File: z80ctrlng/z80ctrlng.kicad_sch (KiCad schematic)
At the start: 54 parts, among them J1 BUS, J10 QWIIC, J11 CLOCK, J2 MICRO_SD, J3 UEXT, J4 SERIAL, J5 3V_LINK, J6 UPDI, J7 UEXT_CS, J8 S1_LINK, J9 S2_LINK, Q4 BSS138, SW1 RESET, SW1 RTC, SW2 BANK_EN, U1 AVR128DB64x-xPT, U1 MCP7940N-xST, U2 MIC5504-3.3YM5, U5 74HCT574, U6 74HCT257, U7 AS6C4008-55PCN, Y1 32kHz

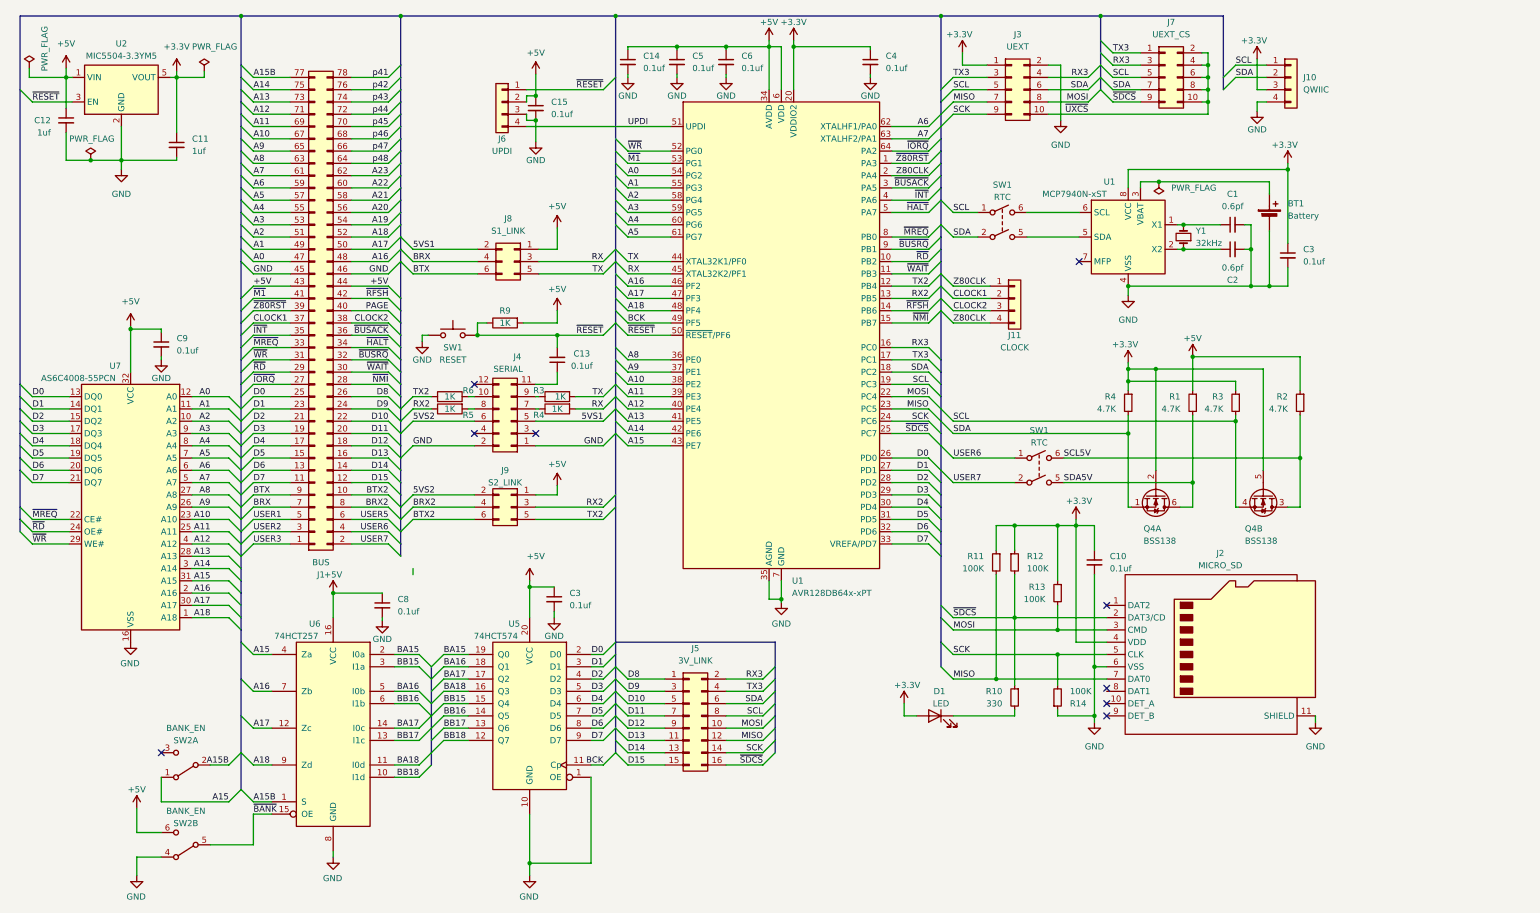
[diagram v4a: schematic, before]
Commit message: Switch to RCBus-80 footprints, JLCPCB preferred components
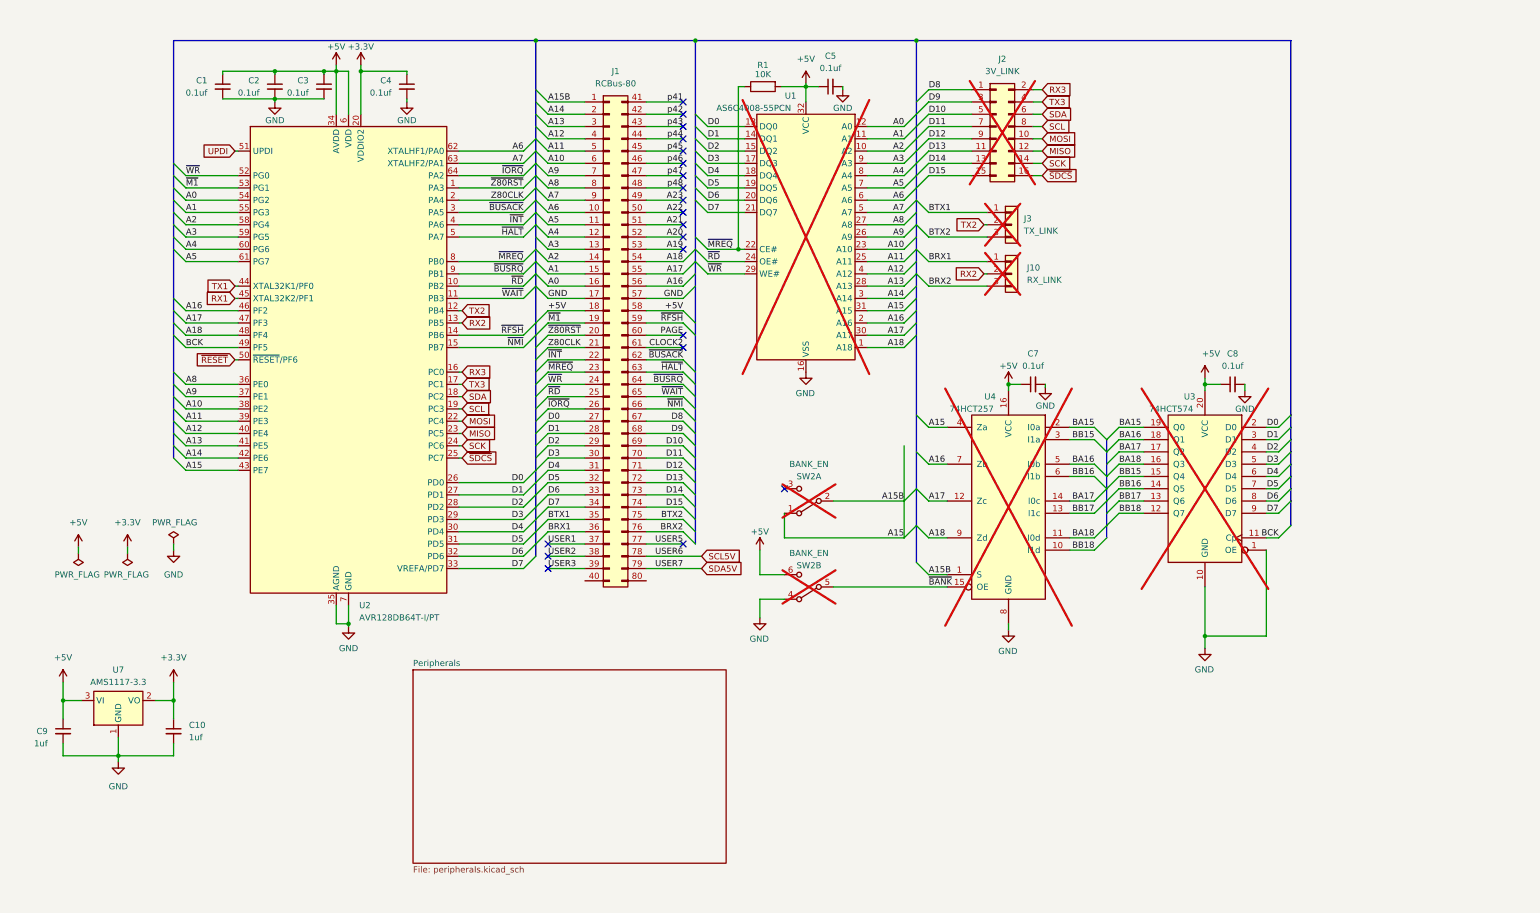
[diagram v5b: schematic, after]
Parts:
- removed BT1: Battery, Battery:BatteryHolder_Keystone_3001_1x12mm, symbol Device:Battery_Cell
- removed C1, C2: 0.6pf, Capacitor_SMD:C_0402_1005Metric, symbol Device:C_Small
- removed C11, C12: 1uf, Capacitor_SMD:C_0402_1005Metric, symbol Device:C_Small
- removed C13, C15, C3: 0.1uf, Capacitor_SMD:C_0402_1005Metric, symbol Device:C_Small
- removed D1: LED, LED_SMD:LED_0805_2012Metric, symbol Device:LED
- removed J1: BUS, Connector_PinHeader_2.54mm:PinHeader_2x39_P2.54mm_Horizontal, symbol Connector_Generic:Conn_02x39_Odd_Even
- removed J10: QWIIC, Custom:JST_SM04B-SRSS-TB_LF__SN_, symbol Connector_Generic:Conn_01x04
- removed J11: CLOCK, Connector_PinHeader_2.54mm:PinHeader_1x04_P2.54mm_Vertical, symbol Connector_Generic:Conn_01x04
- removed J2: MICRO_SD, Connector_Card:microSD_HC_Molex_104031-0811, symbol Connector:Micro_SD_Card_Det2
- removed J3: UEXT, Connector_IDC:IDC-Header_2x05_P2.54mm_Vertical, symbol Connector_Generic:Conn_02x05_Odd_Even
- removed J4: SERIAL, Connector_PinHeader_2.54mm:PinHeader_2x06_P2.54mm_Horizontal, symbol Connector_Generic:Conn_02x06_Odd_Even
- removed J6: UPDI, Connector_PinHeader_2.54mm:PinHeader_1x04_P2.54mm_Horizontal, symbol Connector_Generic:Conn_01x04
- removed J7: UEXT_CS, Connector_PinHeader_2.54mm:PinHeader_2x05_P2.54mm_Vertical, symbol Connector_Generic:Conn_02x05_Odd_Even
- removed J8: S1_LINK, Connector_PinHeader_2.54mm:PinHeader_2x03_P2.54mm_Vertical, symbol Connector_Generic:Conn_02x03_Odd_Even
- removed J9: S2_LINK, Connector_PinHeader_2.54mm:PinHeader_2x03_P2.54mm_Vertical, symbol Connector_Generic:Conn_02x03_Odd_Even
- removed Q4: BSS138, Package_TO_SOT_SMD:SOT-363_SC-70-6, symbol Transistor_FET:FDG6335N
- removed R1, R2, R3, R4: 4.7K, Resistor_SMD:R_0402_1005Metric, symbol Device:R_Small
- removed R10: 330, Resistor_SMD:R_0402_1005Metric, symbol Device:R_Small
- removed R11, R12, R13, R14: 100K, Resistor_SMD:R_0402_1005Metric, symbol Device:R_Small
- removed R3, R4, R5, R6, R9: 1K, Resistor_SMD:R_0402_1005Metric, symbol Device:R
- removed SW1: RESET, Button_Switch_THT:SW_PUSH_6mm, symbol Switch:SW_Push
- removed SW1 (x2): RTC, Custom:SWITCH_011CQN, symbol Switch:SW_DPST
- removed U1: MCP7940N-xST, Package_SO:TSSOP-8_3x3mm_P0.65mm, symbol Timer_RTC:MCP7940N-xST
- removed U2: MIC5504-3.3YM5, Package_TO_SOT_SMD:SOT-23-5, symbol Regulator_Linear:MIC5504-3.3YM5
- removed Y1: 32kHz, Crystal:Crystal_SMD_3215-2Pin_3.2x1.5mm, symbol Device:Crystal_Small
- added C9: 1uf, Capacitor_SMD:C_0402_1005Metric, symbol Device:C_Small
- added J1: RCBus-80, Custom:RCBus-80, symbol Connector_Generic:Conn_02x40_Top_Bottom
- added J10: RX_LINK, Connector_PinHeader_2.54mm:PinHeader_1x03_P2.54mm_Vertical, symbol Connector_Generic:Conn_01x03
- added J3: TX_LINK, Connector_PinHeader_2.54mm:PinHeader_1x03_P2.54mm_Vertical, symbol Connector_Generic:Conn_01x03
- added R1: 10K, Resistor_SMD:R_0402_1005Metric, symbol Device:R
- added U7: AMS1117-3.3, Package_TO_SOT_SMD:SOT-223-3_TabPin2, symbol Regulator_Linear:AMS1117-3.3
- C10: value 0.1uf -> 1uf
- J2: renamed from J5; now not fitted
- SW2: footprint Custom:SWITCH_011CQN -> SamacSys_Parts:JS202011CQN; now not fitted
- U1: renamed from U7; now not fitted
- U2: renamed from U1; value AVR128DB64x-xPT -> AVR128DB64T-I/PT
- U3: renamed from U5; now not fitted
- U4: renamed from U6; now not fitted
- renumbered C14 to C1, C5 to C2, C6 to C3, C9 to C5, C8 to C7, C3 to C8
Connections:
- net A15B is gone; now on net A15: SW2.2 (B), U4.1 (S)
- net +3.3V: now also U7.2 (VO)
- net +5V: now also C9.1, J1.18 (Pin_18), J1.58 (Pin_58), R1.2, U7.3 (VI)
- net A0: now also J1.16 (Pin_16)
- net A1: now also J1.15 (Pin_15)
- net A10: now also J1.6 (Pin_6)
- net A11: now also J1.5 (Pin_5)
- net A12: now also J1.4 (Pin_4)
- net A13: now also J1.3 (Pin_3)
- net A14: now also J1.2 (Pin_2)
- net A15: now also J1.1 (Pin_1)
- net A16: now also J1.56 (Pin_56)
- net A17: now also J1.55 (Pin_55)
- net A18: now also J1.54 (Pin_54)
- net A19: now also J1.53 (Pin_53)
- net A2: now also J1.14 (Pin_14)
- net A20: now also J1.52 (Pin_52)
- net A21: now also J1.51 (Pin_51)
- net A22: now also J1.50 (Pin_50)
- net A23: now also J1.49 (Pin_49)
- net A3: now also J1.13 (Pin_13)
- net A4: now also J1.12 (Pin_12)
- net A5: now also J1.11 (Pin_11)
- net A6: now also J1.10 (Pin_10)
- net A7: now also J1.9 (Pin_9)
- net A8: now also J1.8 (Pin_8)
- net A9: now also J1.7 (Pin_7)
- net BRX2: now also J1.76 (Pin_76), J10.3 (Pin_3)
- net BTX2: now also J1.75 (Pin_75), J3.3 (Pin_3)
- net CLOCK2: now also J1.61 (Pin_61)
- net D0: now also J1.27 (Pin_27)
- net D1: now also J1.28 (Pin_28)
- net D10: now also J1.69 (Pin_69)
- net D11: now also J1.70 (Pin_70)
- net D12: now also J1.71 (Pin_71)
- net D13: now also J1.72 (Pin_72)
- net D14: now also J1.73 (Pin_73)
- net D15: now also J1.74 (Pin_74)
- net D2: now also J1.29 (Pin_29)
- net D3: now also J1.30 (Pin_30)
- net D4: now also J1.31 (Pin_31)
- net D5: now also J1.32 (Pin_32)
- net D6: now also J1.33 (Pin_33)
- net D7: now also J1.34 (Pin_34)
- net D8: now also J1.67 (Pin_67)
- net D9: now also J1.68 (Pin_68)
- net GND: now also C9.2, J1.17 (Pin_17), J1.57 (Pin_57), U7.1 (GND)
- net PAGE: now also J1.60 (Pin_60)
- net RX2: now also J10.2 (Pin_2)
- net SCL5V: now also J1.78 (Pin_78)
- net SDA5V: now also J1.79 (Pin_79)
- net TX2: now also J3.2 (Pin_2)
- net USER1: now also J1.37 (Pin_37)
- net USER2: now also J1.38 (Pin_38)
- net USER3: now also J1.39 (Pin_39)
- net USER5: now also J1.77 (Pin_77)
- net Z80CLK: now also J1.21 (Pin_21)
- net p41: now also J1.41 (Pin_41)
- net p42: now also J1.42 (Pin_42)
- net p43: now also J1.43 (Pin_43)
- net p44: now also J1.44 (Pin_44)
- net p45: now also J1.45 (Pin_45)
- net p46: now also J1.46 (Pin_46)
- net p47: now also J1.47 (Pin_47)
- net p48: now also J1.48 (Pin_48)
- net ~{BUSACK}: now also J1.62 (Pin_62)
- net ~{BUSRQ}: now also J1.64 (Pin_64)
- net ~{HALT}: now also J1.63 (Pin_63)
- net ~{INT}: now also J1.22 (Pin_22)
- net ~{IORQ}: now also J1.26 (Pin_26)
- net ~{M1}: now also J1.19 (Pin_19)
- net ~{MREQ}: now also J1.23 (Pin_23), R1.1
- net ~{NMI}: now also J1.66 (Pin_66)
- net ~{RD}: now also J1.25 (Pin_25)
- net ~{RFSH}: now also J1.59 (Pin_59)
- net ~{WAIT}: now also J1.65 (Pin_65)
- net ~{WR}: now also J1.24 (Pin_24)
- net ~{Z80RST}: now also J1.20 (Pin_20)
- net RX renamed RX1
- net TX renamed TX1
- new net BRX1: J1.36 (Pin_36), J10.1 (Pin_1)
- new net BTX1: J1.35 (Pin_35), J3.1 (Pin_1)
- no-connect marks 9 -> 20
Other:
- added sheet Peripherals (peripherals.kicad_sch)
- moved on the sheet: C1, C2, C3, C4, C5, C7, C8, U2

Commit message: Final touches... I hope
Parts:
- added H1: MountingHole, MountingHole:MountingHole_3.2mm_M3, symbol Mechanical:MountingHole
- C10, C9: footprint Capacitor_SMD:C_0402_1005Metric -> Capacitor_SMD:C_1206_3216Metric
- U2: value AVR128DB64T-I/PT -> AVR128DB64x-xPT
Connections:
- net A15: no longer J1.1 (Pin_1), SW2.2 (B), U4.1 (S)
- net A16: now also U2.47 (PF3); no longer U2.46 (PF2)
- net A17: now also U2.48 (PF4); no longer U2.47 (PF3)
- net A18: now also U2.49 (PF5); no longer U2.48 (PF4)
- net BCK: now also U2.14 (PB6); no longer U2.49 (PF5)
- net ~{RFSH}: no longer U2.14 (PB6)
- net BRX1 renamed RX1B
- net BRX2 renamed RX2B
- net BTX1 renamed TX1B
- net BTX2 renamed TX2B
- net RX1 renamed RXU
- net RX2 renamed RXB
- net RX3 renamed TX3V
- net TX1 renamed TXU
- net TX2 renamed TXB
- net TX3 renamed RX3V
- net ~{SDCS} renamed ~{SS}
- new net A15B: J1.1 (Pin_1), SW2.2 (B), U4.1 (S)
- new net CTS: U2.46 (PF2)

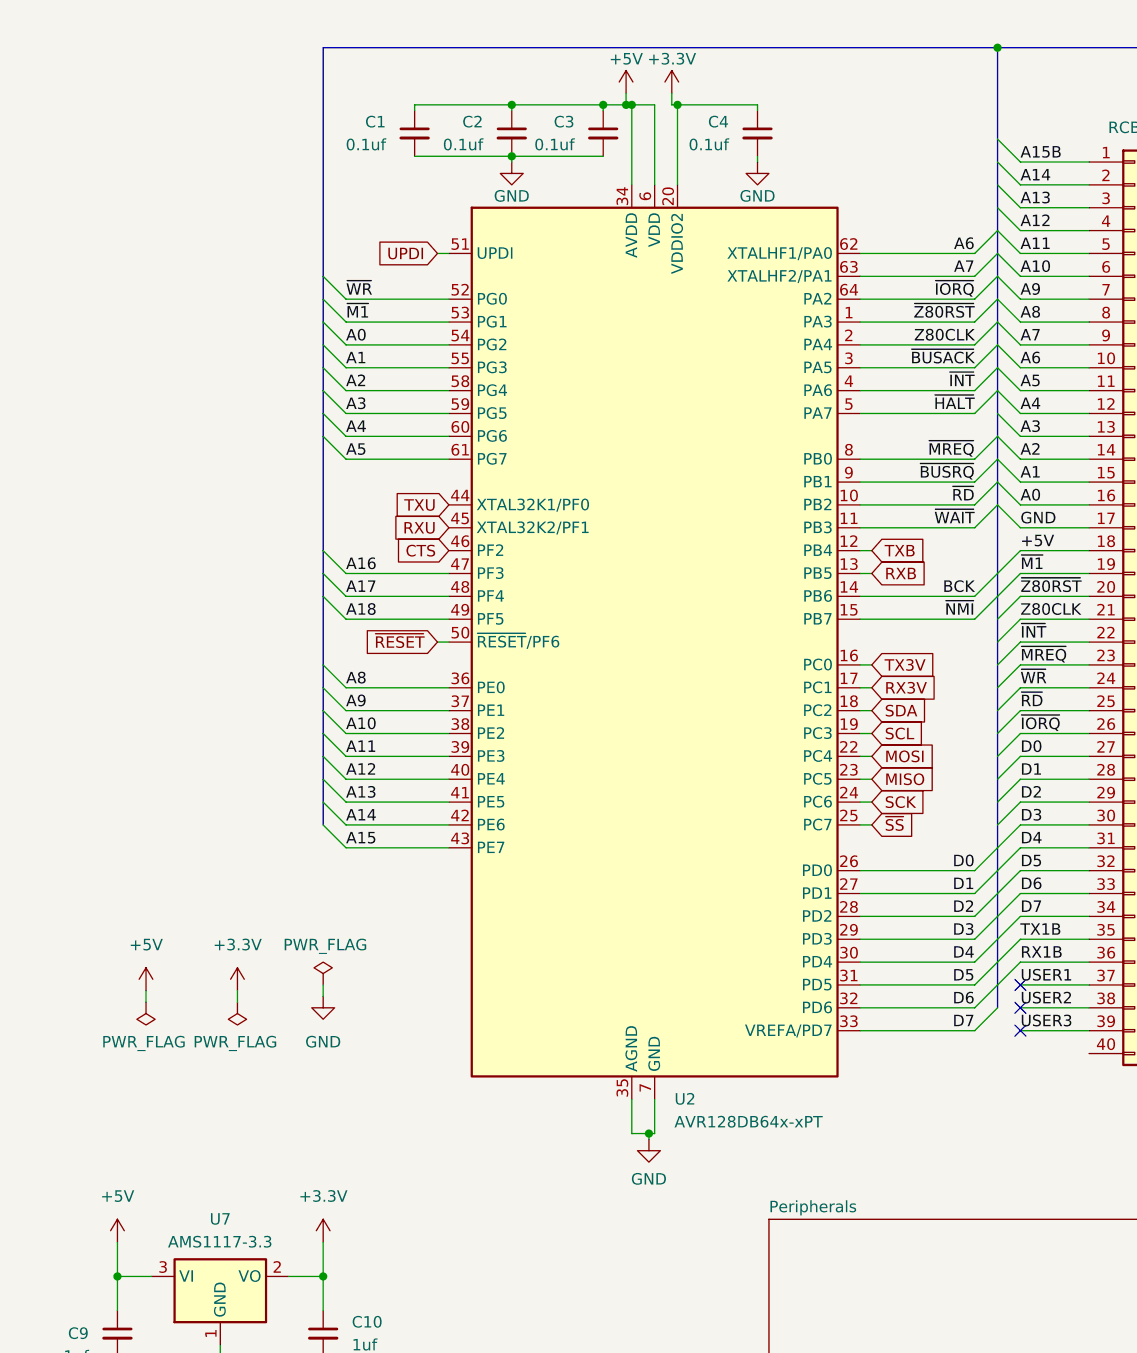
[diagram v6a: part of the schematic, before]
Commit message: Fixing mistakes on RX/TX, better isolation for RTC
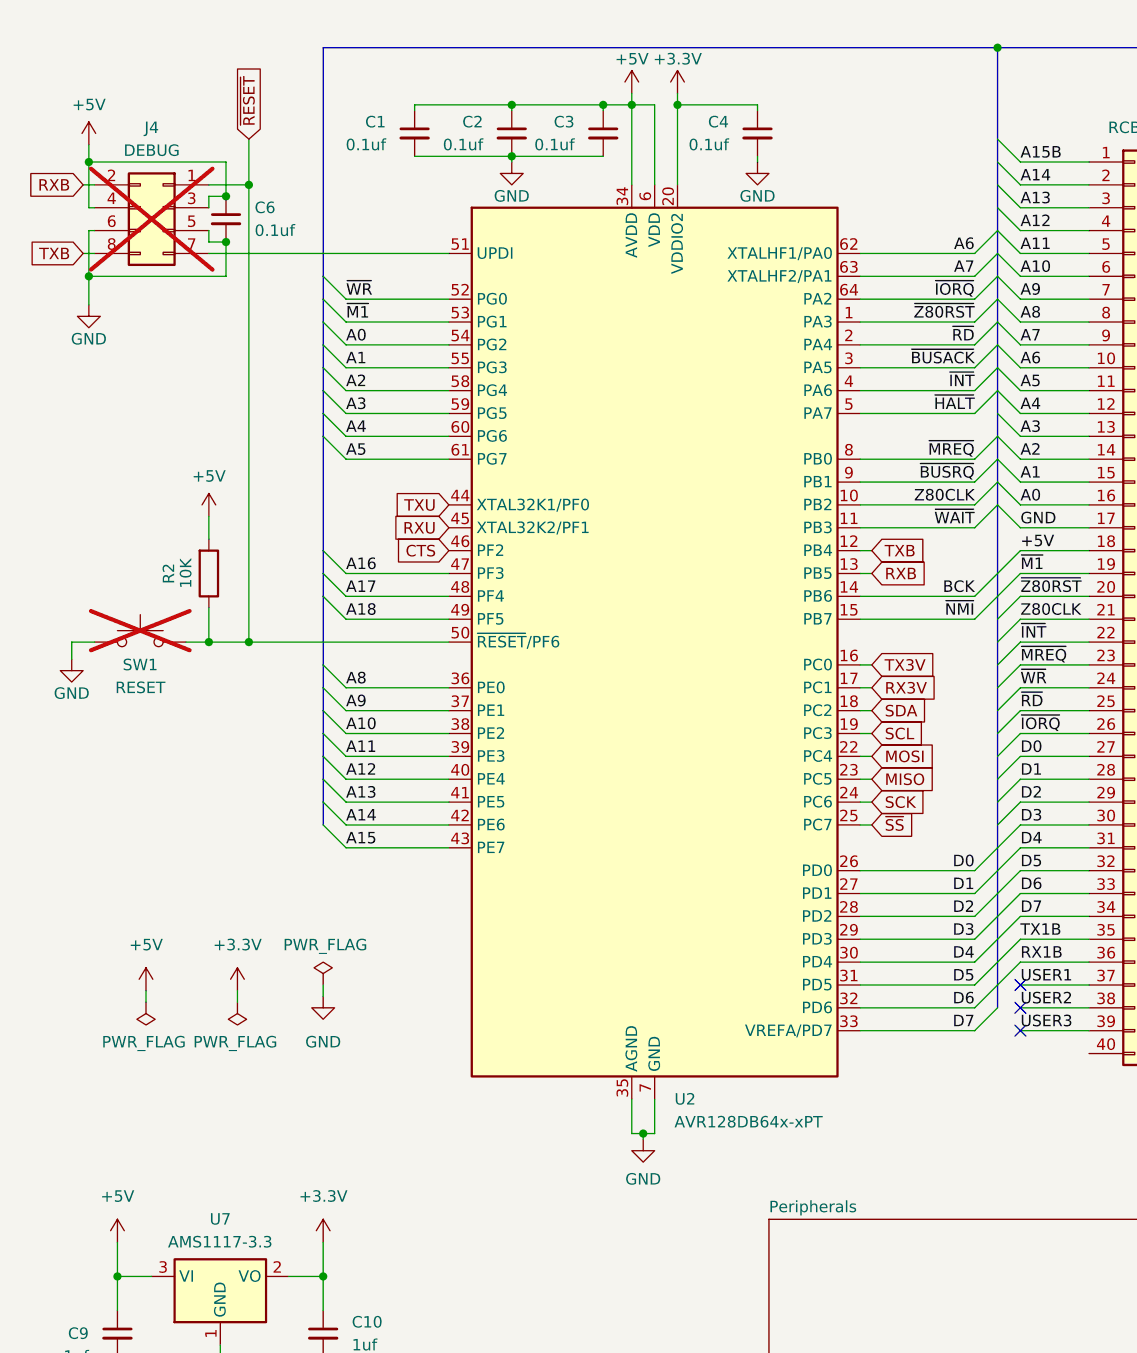
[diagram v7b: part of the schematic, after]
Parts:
- added C6: 0.1uf, Capacitor_SMD:C_0402_1005Metric, symbol Device:C_Small
- added J4: DEBUG, Connector_PinHeader_2.54mm:PinHeader_2x04_P2.54mm_Horizontal, symbol Connector_Generic:Conn_02x04_Odd_Even
- added R2: 10K, Resistor_SMD:R_0402_1005Metric, symbol Device:R
- added SW1: RESET, Button_Switch_THT:SW_Tactile_SPST_Angled_PTS645Vx31-2LFS, symbol Switch:SW_Push
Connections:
- net +5V: now also C6.1, J4.3 (Pin_3), J4.4 (Pin_4), R2.2
- net GND: now also C6.2, J4.5 (Pin_5), J4.6 (Pin_6), SW1.1
- net RXB: now also J4.2 (Pin_2)
- net TXB: now also J4.8 (Pin_8)
- net Z80CLK: now also U2.10 (PB2); no longer U2.2 (PA4)
- net ~{RD}: now also U2.2 (PA4); no longer U2.10 (PB2)
- net ~{RESET}: now also J4.1 (Pin_1), R2.1, SW1.2
- net UPDI: no longer names the net of U2.51 (UPDI)
- net UPDI: now also J4.7 (Pin_7)

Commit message: More final touches o.O
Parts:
- removed R2: 10K, Resistor_SMD:R_0402_1005Metric, symbol Device:R
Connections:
- net CTS is gone; now on net BCK: U2.46 (PF2)
- net BCK: no longer U2.14 (PB6)
- new net ~{SDCS}: U2.14 (PB6)
